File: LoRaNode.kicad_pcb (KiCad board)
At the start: 2 copper layers, 45 x 53 mm, 33 parts, among them J10 D4, J11 A1, J12 A2, J13 A3, J14 D8, J2 Conn_01x03, J4 ISP, J5 Conn_01x06, J6 Conn_01x04, J7 A3, J8 D2, J9 D3, U1 RFM95W-868S2, U4 ATMEGA328P-AU, Y1 8MHz HC5032/4

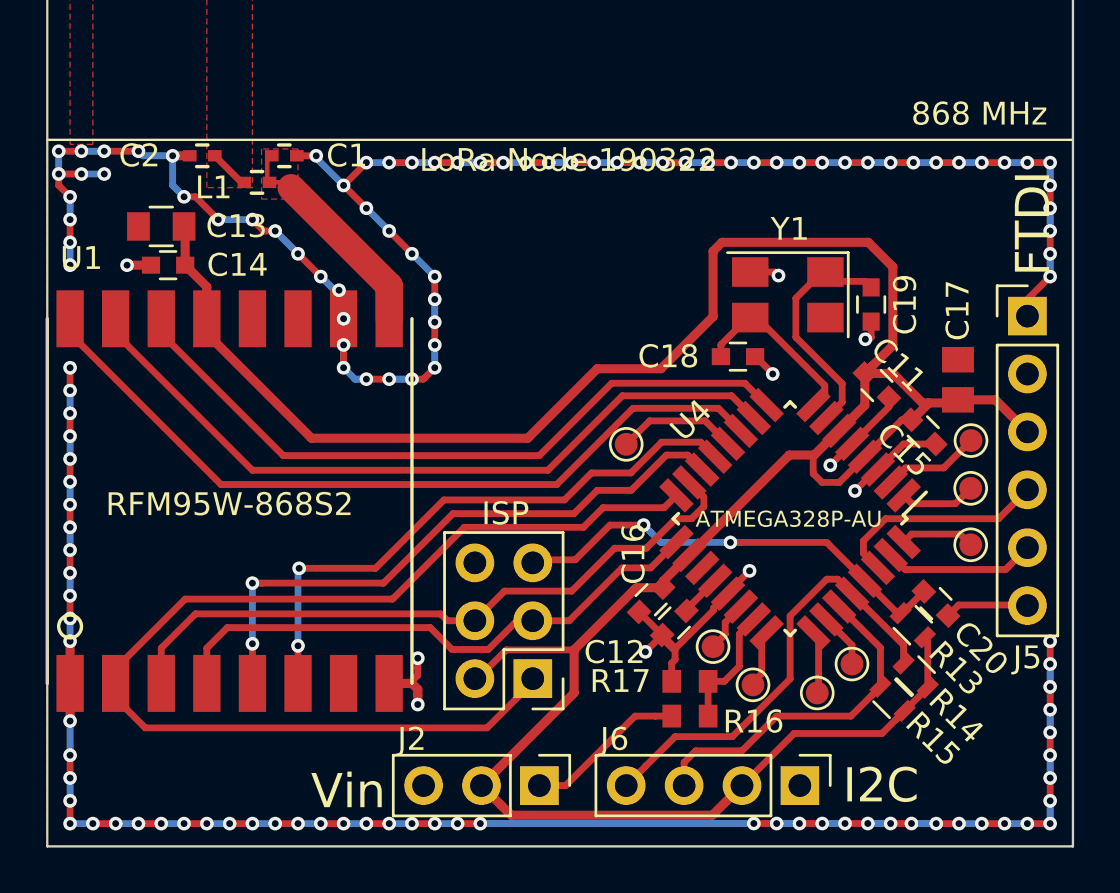
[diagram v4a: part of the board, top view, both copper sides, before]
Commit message: Added more 5 GPIO's and push button
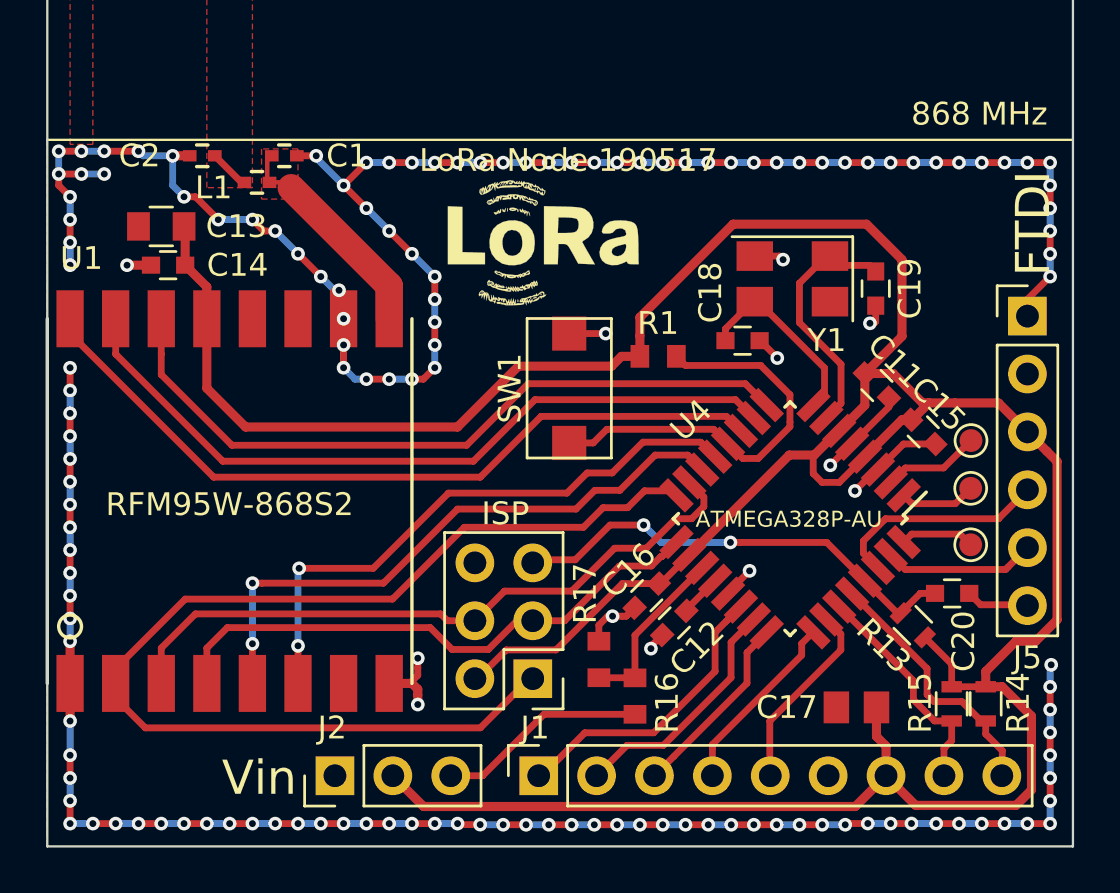
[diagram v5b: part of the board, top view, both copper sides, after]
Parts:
- removed J11: A1, TestPoint:TestPoint_Pad_D1.0mm
- removed J12: A2, TestPoint:TestPoint_Pad_D1.0mm
- removed J13, J7: A3, TestPoint:TestPoint_Pad_D1.0mm
- removed J14: D8, TestPoint:TestPoint_Pad_D1.0mm
- removed J6: Conn_01x04, Pin_Headers:Pin_Header_Straight_1x04_Pitch2.54mm
- added G***: LoRa-Logo-Small, kicad-footprints-master:LoRa-Logo-Small, F.Cu at (149.2, 92.9)
- added J1: Conn_01x09, Connector_PinSocket_2.54mm:PinSocket_1x09_P2.54mm_Vertical, F.Cu at (148.6, 115.9)
- added R1: 100k, Resistor_SMD:R_0603_1608Metric, F.Cu at (153.8, 97.5)
- added SW1: SW_Push, kicad-footprints-master:SMD-PushButton-6x3.6mm, F.Cu at (149.9, 98.9)
- moved C17 15.0 mm to (162.5, 112.9), turned to 180 degrees
- moved J2 8.98 mm to (139.6, 115.9), turned to 90 degrees
- moved R17 4.11 mm to (151.2, 110.8), turned to 90 degrees
- moved R14 3.31 mm to (168.2, 112.7), turned to 270 degrees
- moved R15 2.60 mm to (166.7, 112.7), turned to 270 degrees
- moved R16 2.56 mm to (152.8, 112.4), turned to 90 degrees
- moved C20 0.84 mm to (166.7, 107.9), turned to 0 degrees
- moved C19 0.73 mm to (163.3, 94.5)
- moved C18 0.73 mm to (157.5, 96.8)
- moved Y1 0.73 mm to (159.7, 94.1)
- moved C16 0.26 mm to (153.3, 108.0)
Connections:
- J2 pad 1: /VBAT -> GND
- J2 pad 3: GND -> /VBAT
- R16 pad 2: /A0 -> /A6
- R17 pad 1: /A0 -> /A6
- U4 pad 19: (no net) -> /A6
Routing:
- net +3V3: track 119.9 -> 145.6 mm
- net /D8: track 5.31 -> 18.2 mm
- net /A7: track 2.26 -> 12.9 mm
- net /SCL: track 19.5 -> 11.6 mm
- net /A6: track 0.00 -> 7.63 mm
- net /A3: track 2.42 -> 8.42 mm
- net /A1: track 2.55 -> 8.33 mm
- net /A2: track 3.21 -> 8.58 mm
- net /SDA: track 15.3 -> 10.0 mm
- net /A0: track 5.49 -> 10.7 mm
- net GND: track 184.1 -> 179.9 mm, vias 139 -> 151
- net /VBAT: track 7.07 -> 9.20 mm
- net /DTR: track 3.69 -> 2.78 mm
- net /D5: track 31.1 -> 31.8 mm
- net Net-(C19-Pad1): track 10.4 -> 11.1 mm
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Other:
- net class Default: clearance 0.2 -> 0.25; trace_width 0.2 -> 0.3
- rule trace_clearance: 0.2 -> 0.25
- rule trace_min: 0.2 -> 0.1
- board text added: "LoRa Node 190517"
- board text added: "SCL SDA 3V3 GND A3 A2 A1 A0 A7"
- board text removed: "I2C"
- board text removed: "LoRa Node 190322"
- board text removed: "SCL SDA 3V3 GND"

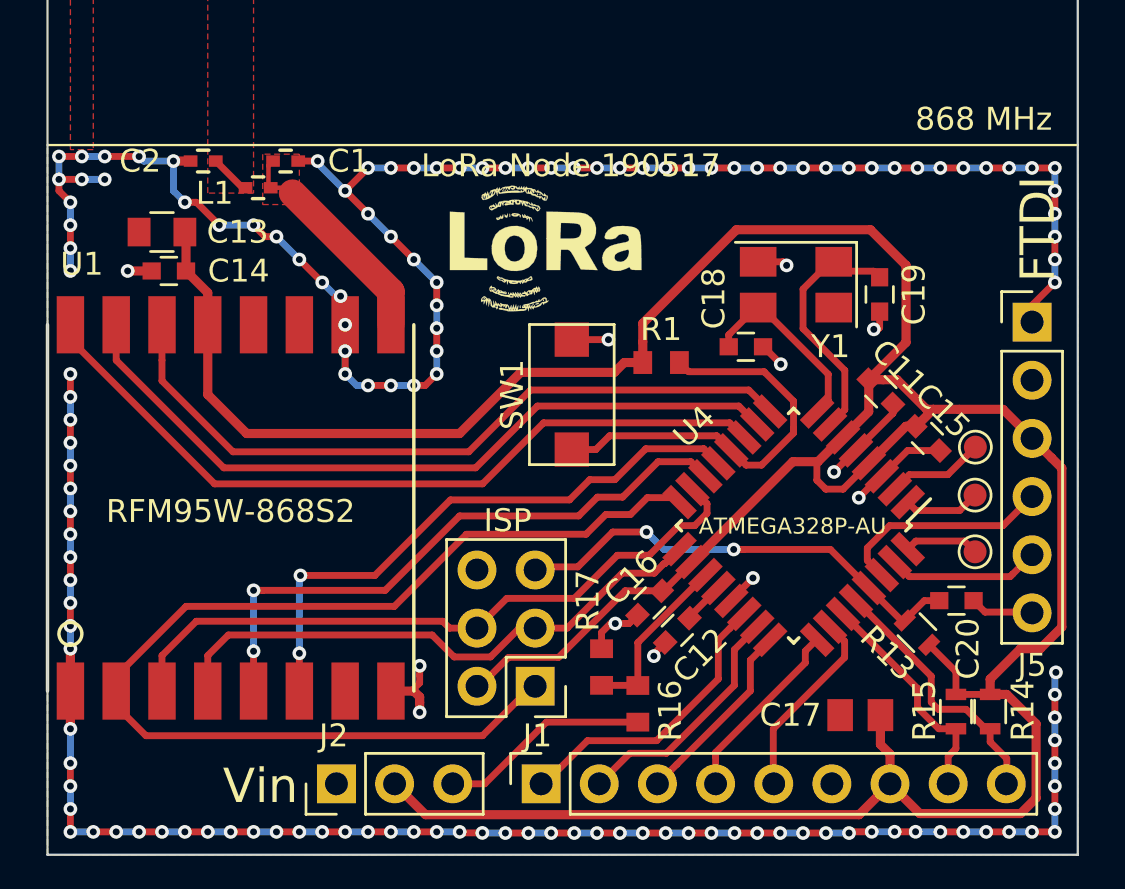
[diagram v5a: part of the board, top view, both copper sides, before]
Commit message: Added LED, changed footprints to actual KiCAD library
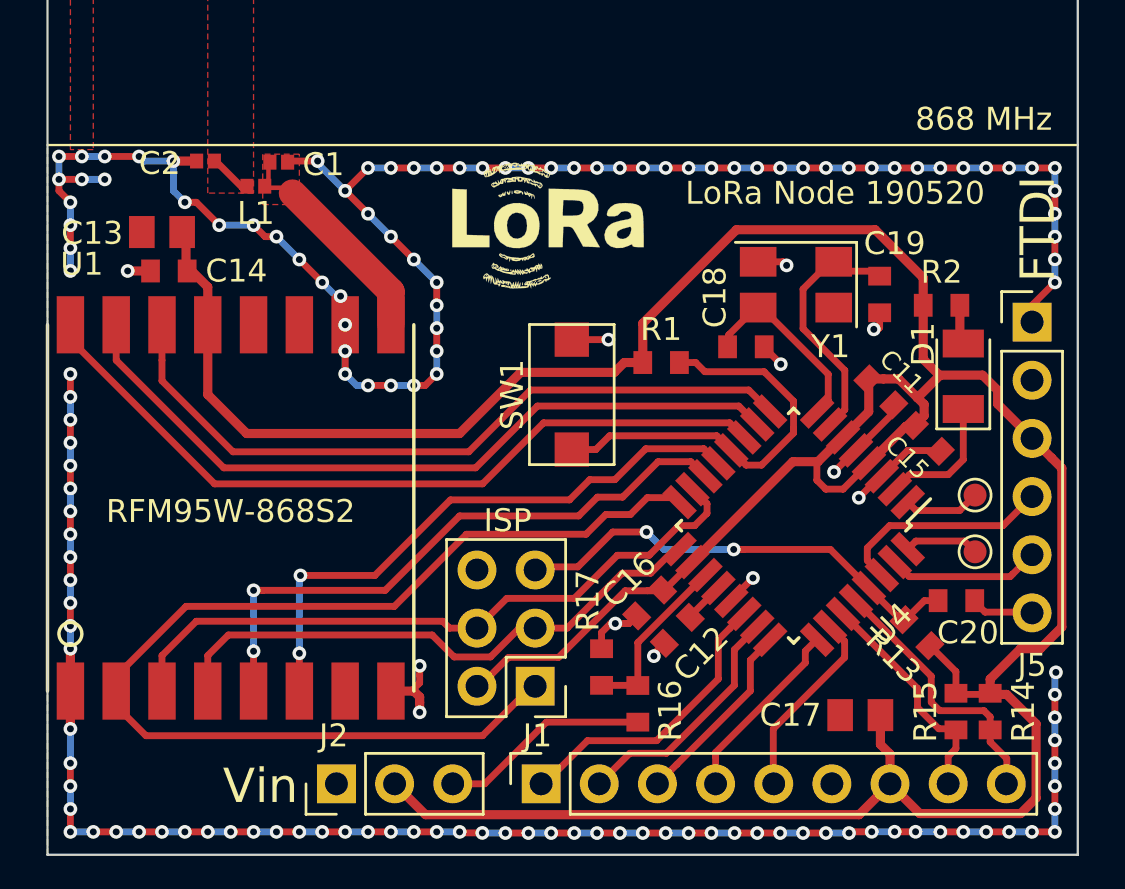
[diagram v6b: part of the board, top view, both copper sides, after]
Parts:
- removed J10: D4, TestPoint:TestPoint_Pad_D1.0mm
- added D1: LED, LED_SMD:LED_1206_3216Metric, F.Cu at (167.0, 98.1)
- added R2: 1k, Resistor_SMD:R_0603_1608Metric, F.Cu at (166.1, 95.0)
- C1, C2: footprint Capacitors_SMD:C_0402 -> Capacitor_SMD:C_0402_1005Metric
- C11, C12, C14, C15, C16, C18, C19, C20: footprint Capacitors_SMD:C_0603 -> Capacitor_SMD:C_0603_1608Metric
- C13: footprint Capacitors_SMD:C_0805 -> Capacitor_SMD:C_0805_2012Metric
- L1: footprint Capacitors_SMD:C_0402 -> Inductor_SMD:L_0402_1005Metric
- R13, R14, R15: footprint Resistors_SMD:R_0603 -> Resistor_SMD:R_0603_1608Metric
- U4: footprint Housings_QFP:TQFP-32_7x7mm_Pitch0.8mm -> Package_QFP:TQFP-32_7x7mm_P0.8mm
- moved G*** 1.00 mm to (149.3, 91.9)
- moved C1 0.30 mm to (137.1, 88.8)
- moved L1 0.12 mm to (136.1, 89.8)
- moved C2 0.10 mm to (133.9, 88.7)
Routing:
- net Net-(D1-Pad2): track 0.00 -> 1.73 mm
- net +3V3: track 145.6 -> 147.1 mm
- net /D4: track 4.28 -> 5.74 mm
- net /SCL: track 11.6 -> 12.1 mm
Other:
- board text added: "LoRa Node 190520"
- board text removed: "LoRa Node 190517"

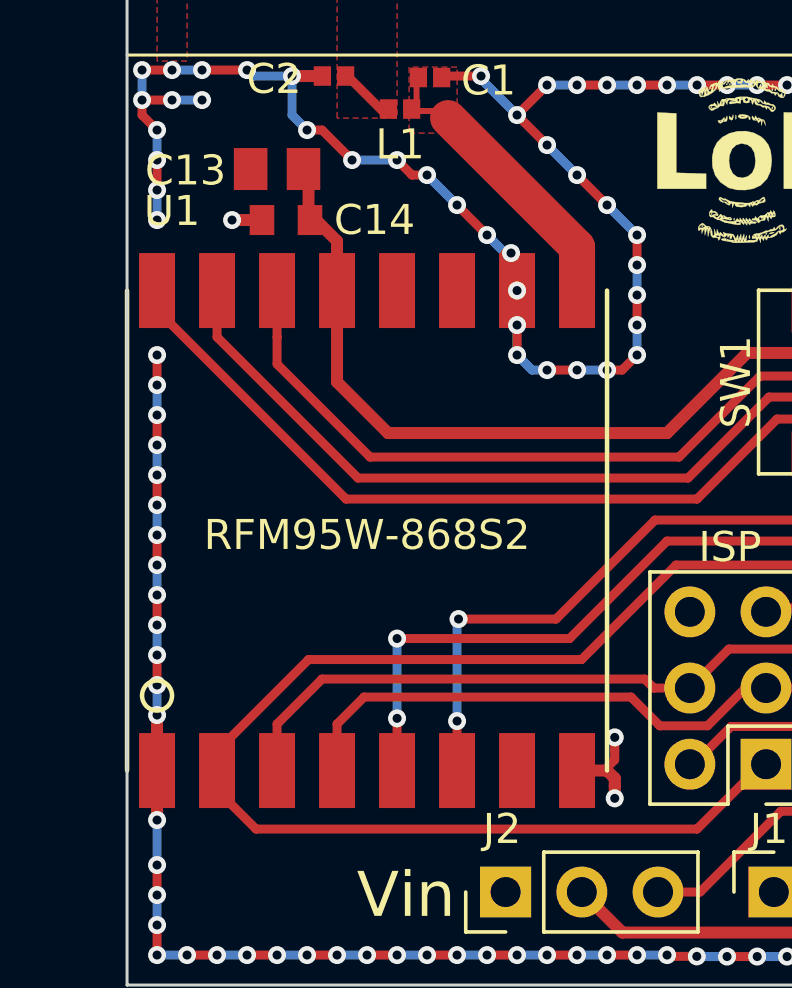
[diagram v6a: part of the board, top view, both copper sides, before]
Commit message: Changed RFM95W footprint
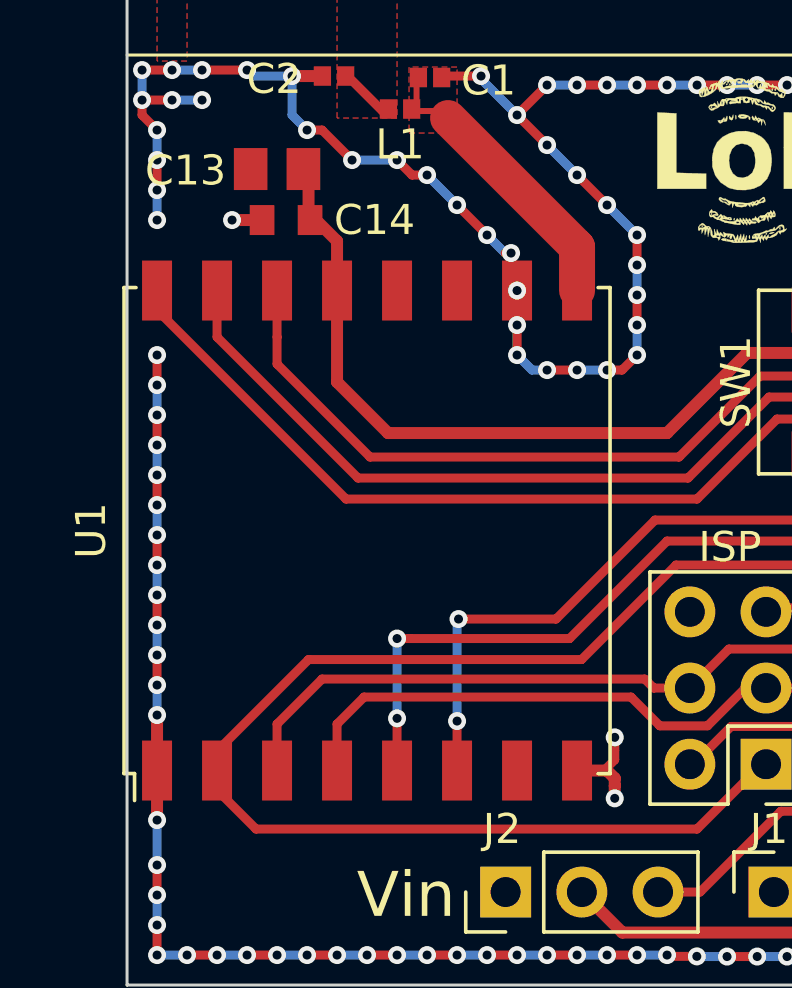
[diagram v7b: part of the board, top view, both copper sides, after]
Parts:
- U1: footprint footprints:RFM95W -> riske:HOPERF_RFM95W_SMD
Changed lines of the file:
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@@
-(kicad_pcb (version 20171130) (host pcbnew "(5.0.2)-1")
+(kicad_pcb (version 20171130) (host pcbnew "(5.1.2)-1")
   (general
     (thickness 1.6)
@@
     (zone_45_only no)
     (trace_min 0.1)
-    (segment_width 0.1)
-    (edge_width 0.1)
     (via_size 0.6)
     (via_drill 0.3)
@@
     (uvia_min_size 0.2)
     (uvia_min_drill 0.1)
+    (edge_width 0.1)
+    (segment_width 0.1)
     (pcb_text_width 0.3)
     (pcb_text_size 1.5 1.5)
@@
     (solder_mask_min_width 0.25)
     (aux_axis_origin 150 50)
-    (visible_elements 7FFFFFFF)
+    (visible_elements 7FFFEFFF)
     (pcbplotparams
       (layerselection 0x010f0_ffffffff)
@@
     (add_net "Net-(C19-Pad1)")
     (add_net "Net-(D1-Pad2)")
-  )
-  (module footprints:RFM95W (layer F.Cu)
-    (at 135 103.85 90)
-    (attr smd)
-    (fp_text reference U1 (at 10.65 -6.5 180) (layer F.SilkS)
-      (effects (font (size 1 1) (thickness 0.15)))
-    )
-    (fp_text value RFM95W-868S2 (at -0.15 0 180) (layer F.SilkS)
-      (effects (font (size 1 1) (thickness 0.15)))
-    )
-    (fp_circle (center -5.5 -7) (end -5.5 -6.5) (layer F.SilkS) (width 0.15))
-    (fp_line (start -8 8) (end 8 8) (layer F.SilkS) (width 0.15))
-    (fp_line (start -8 -8) (end 8 -8) (layer F.SilkS) (width 0.15))
-    (pad 1 smd rect (at -8 -7 90) (size 2.5 1.2) (layers F.Cu F.Paste F.Mask)
-      (net 24 GND))
-    (pad 2 smd rect (at -8 -5 90) (size 2.5 1.2) (layers F.Cu F.Paste F.Mask)
-      (net 2 "/12(**/MOSI)"))
-    (pad 3 smd rect (at -8 -3 90) (size 2.5 1.2) (layers F.Cu F.Paste F.Mask)
-      (net 3 "/11(MISO)"))
-    (pad 4 smd rect (at -8 -1 90) (size 2.5 1.2) (layers F.Cu F.Paste F.Mask)
-      (net 1 "/13(SCK)"))
-    (pad 5 smd rect (at -8 1 90) (size 2.5 1.2) (layers F.Cu F.Paste F.Mask)
-      (net 19 "/10(**/SS)"))
-    (pad 6 smd rect (at -8 3 90) (size 2.5 1.2) (layers F.Cu F.Paste F.Mask)
-      (net 12 /D9))
-    (pad 7 smd rect (at -8 5 90) (size 2.5 1.2) (layers F.Cu F.Paste F.Mask))
-    (pad 8 smd rect (at -8 7 90) (size 2.5 1.2) (layers F.Cu F.Paste F.Mask)
-      (net 24 GND))
-    (pad 9 smd rect (at 8 7 90) (size 2.5 1.2) (layers F.Cu F.Paste F.Mask)
-      (net 5 "Net-(C1-Pad1)"))
-    (pad 10 smd rect (at 8 5 90) (size 2.5 1.2) (layers F.Cu F.Paste F.Mask)
-      (net 24 GND))
-    (pad 11 smd rect (at 8 3 90) (size 2.5 1.2) (layers F.Cu F.Paste F.Mask))
-    (pad 12 smd rect (at 8 1 90) (size 2.5 1.2) (layers F.Cu F.Paste F.Mask))
-    (pad 13 smd rect (at 8 -1 90) (size 2.5 1.2) (layers F.Cu F.Paste F.Mask)
-      (net 4 +3V3))
-    (pad 14 smd rect (at 8 -3 90) (size 2.5 1.2) (layers F.Cu F.Paste F.Mask)
-      (net 17 /D5))
-    (pad 15 smd rect (at 8 -5 90) (size 2.5 1.2) (layers F.Cu F.Paste F.Mask)
-      (net 14 /D6))
-    (pad 16 smd rect (at 8 -7 90) (size 2.5 1.2) (layers F.Cu F.Paste F.Mask)
-      (net 13 /D7))
-    (model C:/Engineering/KiCAD_Libraries/3D/Modules/VRML/RFM95W.wrl
-      (at (xyz 0 0 0))
-      (scale (xyz 1 1 1))
-      (rotate (xyz 0 0 0))
-    )
   )
   (module Pin_Headers:Pin_Header_Straight_2x03_Pitch2.54mm (layer F.Cu)
@@
     )
   )
+  (module riske:HOPERF_RFM95W_SMD (layer F.Cu)
+    (at 135 103.85 90)
+    (descr "Low Power Long Range Transceiver Module SMD-16 (https://www.hoperf.com/data/upload/portal/20181127/5bfcbea20e9ef.pdf)")
+    (tags "LoRa Low Power Long Range Transceiver Module")
+    (attr smd)
+    (fp_text reference U1 (at 0 -9.2 90) (layer F.SilkS)
+      (effects (font (size 1 1) (thickness 0.15)))
+    )
+    (fp_text value RFM95W-868S2 (at 0 9.5 90) (layer F.Fab)
+      (effects (font (size 1 1) (thickness 0.15)))
+    )
+    (fp_line (start -7 -8) (end 8 -8) (layer F.Fab) (width 0.1))
+    (fp_line (start 8 8) (end 8 -8) (layer F.Fab) (width 0.1))
+    (fp_line (start -8 8) (end 8 8) (layer F.Fab) (width 0.1))
+    (fp_line (start -8 8) (end -8 -7) (layer F.Fab) (width 0.1))
+    (fp_text user %R (at 0 0 90) (layer F.Fab)
+      (effects (font (size 1 1) (thickness 0.15)))
+    )
+    (fp_line (start -9.25 -8.25) (end 9.25 -8.25) (layer F.CrtYd) (width 0.05))
+    (fp_line (start 9.25 -8.25) (end 9.25 8.25) (layer F.CrtYd) (width 0.05))
+    (fp_line (start -9.25 8.25) (end 9.25 8.25) (layer F.CrtYd) (width 0.05))
+    (fp_line (start -9.25 8.25) (end -9.25 -8.25) (layer F.CrtYd) (width 0.05))
+    (fp_line (start -8.1 -8.1) (end 8.1 -8.1) (layer F.SilkS) (width 0.12))
+    (fp_line (start 8.1 -8.1) (end 8.1 -7.7) (layer F.SilkS) (width 0.12))
+    (fp_line (start -8.1 7.7) (end -8.1 8.1) (layer F.SilkS) (width 0.12))
+    (fp_line (start -8.1 8.1) (end 8.1 8.1) (layer F.SilkS) (width 0.12))
+    (fp_line (start 8.1 8.1) (end 8.1 7.7) (layer F.SilkS) (width 0.12))
+    (fp_line (start -8.1 -8.1) (end -8.1 -7.75) (layer F.SilkS) (width 0.12))
+    (fp_line (start -8.1 -7.75) (end -9 -7.75) (layer F.SilkS) (width 0.12))
+    (fp_line (start -7 -8) (end -8 -7) (layer F.Fab) (width 0.1))
+    (pad 1 smd rect (at -8 -7 90) (size 2 1) (layers F.Cu F.Paste F.Mask)
+      (net 24 GND))
+    (pad 2 smd rect (at -8 -5 90) (size 2 1) (layers F.Cu F.Paste F.Mask)
+      (net 2 "/12(**/MOSI)"))
+    (pad 3 smd rect (at -8 -3 90) (size 2 1) (layers F.Cu F.Paste F.Mask)
+      (net 3 "/11(MISO)"))
+    (pad 4 smd rect (at -8 -1 90) (size 2 1) (layers F.Cu F.Paste F.Mask)
+      (net 1 "/13(SCK)"))
+    (pad 5 smd rect (at -8 1 90) (size 2 1) (layers F.Cu F.Paste F.Mask)
+      (net 19 "/10(**/SS)"))
+    (pad 6 smd rect (at -8 3 90) (size 2 1) (layers F.Cu F.Paste F.Mask)
+      (net 12 /D9))
+    (pad 7 smd rect (at -8 5 90) (size 2 1) (layers F.Cu F.Paste F.Mask))
+    (pad 8 smd rect (at -8 7 90) (size 2 1) (layers F.Cu F.Paste F.Mask)
+      (net 24 GND))
+    (pad 9 smd rect (at 8 7 90) (size 2 1) (layers F.Cu F.Paste F.Mask)
+      (net 5 "Net-(C1-Pad1)"))
+    (pad 10 smd rect (at 8 5 90) (size 2 1) (layers F.Cu F.Paste F.Mask)
+      (net 24 GND))
+    (pad 11 smd rect (at 8 3 90) (size 2 1) (layers F.Cu F.Paste F.Mask))
+    (pad 12 smd rect (at 8 1 90) (size 2 1) (layers F.Cu F.Paste F.Mask))
+    (pad 13 smd rect (at 8 -1 90) (size 2 1) (layers F.Cu F.Paste F.Mask)
+      (net 4 +3V3))
+    (pad 14 smd rect (at 8 -3 90) (size 2 1) (layers F.Cu F.Paste F.Mask)
+      (net 17 /D5))
+    (pad 15 smd rect (at 8 -5 90) (size 2 1) (layers F.Cu F.Paste F.Mask)
+      (net 14 /D6))
+    (pad 16 smd rect (at 8 -7 90) (size 2 1) (layers F.Cu F.Paste F.Mask)
+      (net 13 /D7))
+    (model ${KISYS3DMOD}/RF_Module.3dshapes/HOPERF_RFM9XW_SMD.wrl
+      (at (xyz 0 0 0))
+      (scale (xyz 1 1 1))
+      (rotate (xyz 0 0 0))
+    )
+    (model "E:/download/RFM95 LoRa v15.step"
+      (offset (xyz -8 8 0))
+      (scale (xyz 1 1 1))
+      (rotate (xyz -90 0 0))
+    )
+  )
